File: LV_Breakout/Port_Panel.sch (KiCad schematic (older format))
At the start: 24 parts, among them J1 DB9_Male_MountingHoles, J10 TE 776228-1, J2 B3B-PH-K-S(LF)(SN), J3 Conn_02x03_Odd_Even, J4 LD09S13A4GX00LF, J5 USB_B, J6 RJ45, J7 B6B-XH-A(LF)(SN), J8 B10B-PHDSS(LF)(SN), J9 RJ45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

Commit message: change port panel
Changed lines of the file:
@@
 	9425 2775 8750 2775
 Wire Wire Line
+	10050 2125 10625 2125
+Wire Wire Line
+	10050 2925 10625 2925
+Wire Wire Line
 	10050 1325 10625 1325
 Wire Wire Line
-	10050 1225 10625 1225
-Wire Wire Line
-	10050 1125 10625 1125
-Wire Wire Line
-	10050 1025 10625 1025
-Wire Wire Line
-	10625 925  10050 925
-Wire Wire Line
-	10625 825  10050 825
-Text Label 10050 825  0    50   ~ 0
+	10050 2025 10625 2025
+Wire Wire Line
+	10625 2825 10050 2825
+Wire Wire Line
+	10625 2725 10050 2725
+Text Label 10050 2725 0    50   ~ 0
 Sensor_1
-Text Label 10050 925  0    50   ~ 0
+Text Label 10050 2825 0    50   ~ 0
 Sensor_2
-Text Label 10050 1025 0    50   ~ 0
+Text Label 10050 2025 0    50   ~ 0
 Sensor_3
-Text Label 10050 1125 0    50   ~ 0
+Text Label 10050 1325 0    50   ~ 0
 Sensor_4
-Text Label 10050 1225 0    50   ~ 0
+Text Label 10050 2925 0    50   ~ 0
 Sensor_5
-Text Label 10050 1325 0    50   ~ 0
+Text Label 10050 2125 0    50   ~ 0
 Sensor_6
 Text Label 3000 2675 2    50   ~ 0
@@
 Sensor_7
 Wire Wire Line
-	10625 1625 10050 1625
-Text Label 10050 1825 0    50   ~ 0
+	10625 2225 10050 2225
+Text Label 10050 2625 0    50   ~ 0
 CAN+
 Wire Wire Line
@@
 	10050 1525 10625 1525
 Wire Wire Line
-	10050 1725 10625 1725
-Text Label 10050 1725 0    50   ~ 0
+	10050 3025 10625 3025
+Text Label 10050 3025 0    50   ~ 0
 Sensor_10
-Text Label 10050 1625 0    50   ~ 0
+Text Label 10050 2225 0    50   ~ 0
 Sensor_9
 Text Label 10050 1525 0    50   ~ 0
@@
 Sensor_7
 Wire Wire Line
-	10050 1825 10625 1825
-Text Label 10050 2025 0    50   ~ 0
+	10050 2625 10625 2625
+Text Label 10050 2525 0    50   ~ 0
 CAN-
 Wire Wire Line
@@
 L power:GND #PWR026
 U 1 1 5E62FDAB
-P 10275 3025
-F 0 "#PWR026" H 10275 2775 50  0001 C CNN
-F 1 "GND" H 10280 2852 50  0000 C CNN
-F 2 "" H 10275 3025 50  0001 C CNN
-F 3 "" H 10275 3025 50  0001 C CNN
-	1    10275 3025
-	1    0    0    -1
-$EndComp
-Wire Wire Line
-	10275 3025 10625 3025
-Wire Wire Line
-	10625 2925 10275 2925
-Wire Wire Line
-	10275 2925 10275 3025
-Connection ~ 10275 3025
-Wire Wire Line
-	10625 2825 10275 2825
-Wire Wire Line
-	10275 2825 10275 2925
-Connection ~ 10275 2925
-Wire Wire Line
-	10625 2725 10275 2725
-Wire Wire Line
-	10275 2725 10275 2825
-Connection ~ 10275 2825
+P 9875 1225
+F 0 "#PWR026" H 9875 975 50  0001 C CNN
+F 1 "GND" H 9880 1052 50  0000 C CNN
+F 2 "" H 9875 1225 50  0001 C CNN
+F 3 "" H 9875 1225 50  0001 C CNN
+	1    9875 1225
+	1    0    0    -1
+$EndComp
+Wire Wire Line
+	9875 1225 10625 1225
+Wire Wire Line
+	10625 1125 9875 1125
+Wire Wire Line
+	9875 1125 9875 1225
+Connection ~ 9875 1225
+Wire Wire Line
+	10625 1025 9875 1025
+Wire Wire Line
+	9875 1025 9875 1125
+Connection ~ 9875 1125
+Wire Wire Line
+	10625 925  9875 925
+Wire Wire Line
+	9875 925  9875 1025
+Connection ~ 9875 1025
+Text Label 10050 2425 0    50   ~ 0
+RINEHART_RX
+Wire Wire Line
+	10050 2425 10625 2425
 Text Label 10050 2325 0    50   ~ 0
-RINEHART_RX
+RINEHART_TX
 Wire Wire Line
 	10050 2325 10625 2325
-Text Label 10050 2225 0    50   ~ 0
-RINEHART_TX
-Wire Wire Line
-	10050 2225 10625 2225
-Text Label 10050 2425 0    50   ~ 0
+Text Label 10050 1725 0    50   ~ 0
 BMS_FAULT
 Wire Wire Line
-	10050 2425 10625 2425
+	10050 1725 10625 1725
 Text Label 10050 1925 0    50   ~ 0
 CAN+
 Wire Wire Line
-	10050 2025 10625 2025
-Text Label 10050 2125 0    50   ~ 0
+	10050 2525 10625 2525
+Text Label 10050 1825 0    50   ~ 0
 CAN-
 Wire Wire Line
-	10050 2125 10625 2125
+	10050 1825 10625 1825
 $Comp
 L Connector_Generic:Conn_01x06 J7
@@
 Text Notes 5975 750  0    50   ~ 0
 Serial Port\nfor RineHart
-Text Notes 10325 725  0    50   ~ 0
+Text Notes 11625 675  0    50   ~ 0
 Main Ampseal
-Text Label 10050 2525 0    50   ~ 0
+Text Label 10050 1625 0    50   ~ 0
 EMUS_TX+
-Text Label 10050 2625 0    50   ~ 0
+Text Label 10050 825  0    50   ~ 0
 EMUS_TX-
-Text Notes 11075 2625 0    50   ~ 0
+Text Notes 10825 3550 0    50   ~ 0
 EMUS TX- is for \nEMUS Current Monitor RX
 Wire Wire Line
-	10625 2525 10050 2525
-Wire Wire Line
-	10625 2625 10050 2625
+	10625 1625 10050 1625
+Wire Wire Line
+	10625 825  10050 825
 $Comp
 L Device:R R1

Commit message: Updated PCB Layout
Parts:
- added Q1: PSMN5R2-60YL, Package_TO_SOT_SMD:LFPAK56, symbol Transistor_FET:PSMN5R2-60YL
- added R5: 100, Resistor_SMD:R_0603_1608Metric_Pad1.05x0.95mm_HandSolder, symbol Device:R
- J8: value B10B-PHDSS(LF)(SN) -> B12B-PUDSS-1(LF)(SN); footprint Connector_JST:JST_PHD_B10B-PHDSS_2x05_P2.00mm_Vertical -> Connector_JST:JST_PHD_B12B-PHDSS_2x06_P2.00mm_Vertical; symbol Connector_Generic:Conn_02x05_Counter_Clockwise -> Connector_Generic:Conn_02x06_Counter_Clockwise
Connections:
- net labels added: EMUS_Curr1, EMUS_Curr2, EMUS_Curr3, FAN_OUT, FAN_SIG
- net labels removed: BMS_USB_GND, EMUS_TX+, EMUS_TX-, Sensor_10, Sensor_9
- wire segments 137 -> 146
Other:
- note added: "fan control\n"
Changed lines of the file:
@@
 	3000 2475 2600 2475
-Wire Wire Line
-	3000 2575 2600 2575
 Wire Wire Line
 	3000 2675 2600 2675
@@
 $EndComp
 $Comp
-L Connector_Generic:Conn_02x05_Counter_Clockwise J8
+L Connector_Generic:Conn_02x06_Counter_Clockwise J8
 U 1 1 5E5B056E
 P 8450 2775
 F 0 "J8" H 8500 3192 50  0000 C CNN
-F 1 "B10B-PHDSS(LF)(SN)" H 8500 3101 50  0000 C CNN
-F 2 "Connector_JST:JST_PHD_B10B-PHDSS_2x05_P2.00mm_Vertical" H 8450 2775 50  0001 C CNN
+F 1 "B12B-PUDSS-1(LF)(SN)" H 8500 3101 50  0000 C CNN
+F 2 "Connector_JST:JST_PHD_B12B-PHDSS_2x06_P2.00mm_Vertical" H 8450 2775 50  0001 C CNN
 F 3 "~" H 8450 2775 50  0001 C CNN
 	1    8450 2775
 	1    0    0    -1
 $EndComp
+Wire Wire Line
+	7650 2575 8250 2575
 Text Label 7650 2575 0    50   ~ 0
-BMS_USB_GND
-Wire Wire Line
-	7650 2575 8250 2575
+BMS_USB+
+Wire Wire Line
+	7650 2675 8250 2675
 Text Label 7650 2675 0    50   ~ 0
-BMS_USB+
-Wire Wire Line
-	7650 2675 8250 2675
-Text Label 7650 2775 0    50   ~ 0
 BMS_USB-
 Wire Wire Line
 	7650 2775 8250 2775
-Text Label 7650 2875 0    50   ~ 0
+Text Label 9275 3075 2    50   ~ 0
 BMS_FAULT
-Wire Wire Line
-	7650 2875 8250 2875
 Text Label 7650 2975 0    50   ~ 0
 CAN+
@@
 L power:GND #PWR025
 U 1 1 5E5C1626
-P 9425 2775
-F 0 "#PWR025" H 9425 2525 50  0001 C CNN
-F 1 "GND" H 9430 2602 50  0000 C CNN
-F 2 "" H 9425 2775 50  0001 C CNN
-F 3 "" H 9425 2775 50  0001 C CNN
-	1    9425 2775
-	1    0    0    -1
-$EndComp
-Text Label 9275 2875 2    50   ~ 0
+P 7550 3075
+F 0 "#PWR025" H 7550 2825 50  0001 C CNN
+F 1 "GND" H 7555 2902 50  0000 C CNN
+F 2 "" H 7550 3075 50  0001 C CNN
+F 3 "" H 7550 3075 50  0001 C CNN
+	1    7550 3075
+	1    0    0    -1
+$EndComp
+Text Label 7650 2775 0    50   ~ 0
 CAN-
 Wire Wire Line
@@
 Wire Wire Line
 	10625 2725 10050 2725
-Text Label 10050 2725 0    50   ~ 0
+Text Label 10050 2825 0    50   ~ 0
 Sensor_1
-Text Label 10050 2825 0    50   ~ 0
+Text Label 10050 2225 0    50   ~ 0
 Sensor_2
 Text Label 10050 2025 0    50   ~ 0
@@
 Text Label 10050 2125 0    50   ~ 0
 Sensor_6
-Text Label 3000 2675 2    50   ~ 0
-Sensor_10
-Text Label 3000 2575 2    50   ~ 0
-Sensor_9
 Text Label 3000 2475 2    50   ~ 0
 Sensor_8
@@
 Wire Wire Line
 	10050 3025 10625 3025
-Text Label 10050 3025 0    50   ~ 0
-Sensor_10
-Text Label 10050 2225 0    50   ~ 0
-Sensor_9
 Text Label 10050 1525 0    50   ~ 0
 Sensor_8
-Text Label 10050 1425 0    50   ~ 0
-Sensor_7
 Wire Wire Line
 	10050 2625 10625 2625
-Text Label 10050 2525 0    50   ~ 0
+Text Label 10050 2725 0    50   ~ 0
 CAN-
 Wire Wire Line
@@
 	9875 925  9875 1025
 Connection ~ 9875 1025
-Text Label 10050 2425 0    50   ~ 0
+Text Label 10050 1625 0    50   ~ 0
 RINEHART_RX
 Wire Wire Line
 	10050 2425 10625 2425
-Text Label 10050 2325 0    50   ~ 0
+Text Label 10050 825  0    50   ~ 0
 RINEHART_TX
 Wire Wire Line
 	10050 2325 10625 2325
-Text Label 10050 1725 0    50   ~ 0
+Text Label 10050 2525 0    50   ~ 0
 BMS_FAULT
 Wire Wire Line
 	10050 1725 10625 1725
+Text Label 10050 1825 0    50   ~ 0
+CAN+
+Wire Wire Line
+	10050 2525 10625 2525
 Text Label 10050 1925 0    50   ~ 0
-CAN+
-Wire Wire Line
-	10050 2525 10625 2525
-Text Label 10050 1825 0    50   ~ 0
 CAN-
 Wire Wire Line
@@
 L power:+12V #PWR024
 U 1 1 5E6CC3D5
-P 9425 2675
-F 0 "#PWR024" H 9425 2525 50  0001 C CNN
-F 1 "+12V" H 9440 2848 50  0000 C CNN
-F 2 "" H 9425 2675 50  0001 C CNN
-F 3 "" H 9425 2675 50  0001 C CNN
-	1    9425 2675
-	1    0    0    -1
-$EndComp
-Wire Wire Line
-	8750 2675 9425 2675
+P 9425 2775
+F 0 "#PWR024" H 9425 2625 50  0001 C CNN
+F 1 "+12V" H 9440 2948 50  0000 C CNN
+F 2 "" H 9425 2775 50  0001 C CNN
+F 3 "" H 9425 2775 50  0001 C CNN
+	1    9425 2775
+	1    0    0    -1
+$EndComp
 Text Label 7950 1275 0    50   ~ 0
 SDA
@@
 Text Notes 5975 750  0    50   ~ 0
 Serial Port\nfor RineHart
-Text Notes 11625 675  0    50   ~ 0
+Text Notes 10100 625  0    50   ~ 0
 Main Ampseal
-Text Label 10050 1625 0    50   ~ 0
-EMUS_TX+
-Text Label 10050 825  0    50   ~ 0
-EMUS_TX-
-Text Notes 10825 3550 0    50   ~ 0
+Text Label 9250 2675 2    50   ~ 0
+EMUS_Curr2
+Text Label 10050 2325 0    50   ~ 0
+EMUS_Curr1
+Text Notes 10100 3375 0    50   ~ 0
 EMUS TX- is for \nEMUS Current Monitor RX
 Wire Wire Line
@@
 Wire Wire Line
 	2975 2175 2600 2175
+Text Notes 8200 5475 0    50   ~ 0
+fan control\n
+Text Label 3000 2675 2    50   ~ 0
+FAN_SIG
+Text Label 8025 5675 0    50   ~ 0
+FAN_SIG
+Wire Wire Line
+	8025 5675 8475 5675
+$Comp
+L Device:R R5
+U 1 1 5E5C2565
+P 8475 5825
+F 0 "R5" H 8545 5871 50  0000 L CNN
+F 1 "100" H 8545 5780 50  0000 L CNN
+F 2 "Resistor_SMD:R_0603_1608Metric_Pad1.05x0.95mm_HandSolder" V 8405 5825 50  0001 C CNN
+F 3 "~" H 8475 5825 50  0001 C CNN
+	1    8475 5825
+	1    0    0    -1
+$EndComp
+Connection ~ 8475 5675
+Wire Wire Line
+	8475 5675 8625 5675
+$Comp
+L power:GND #PWR0101
+U 1 1 5E5C32FB
+P 8925 6100
+F 0 "#PWR0101" H 8925 5850 50  0001 C CNN
+F 1 "GND" H 8930 5927 50  0000 C CNN
+F 2 "" H 8925 6100 50  0001 C CNN
+F 3 "" H 8925 6100 50  0001 C CNN
+	1    8925 6100
+	1    0    0    -1
+$EndComp
+Wire Wire Line
+	8475 5975 8475 6100
+Wire Wire Line
+	8475 6100 8925 6100
+Wire Wire Line
+	8925 6100 8925 5875
+Connection ~ 8925 6100
+Text Label 8925 5250 0    50   ~ 0
+FAN_OUT
+Wire Wire Line
+	8925 5250 8925 5475
+Text Label 10050 3025 0    50   ~ 0
+FAN_OUT
+$Comp
+L Transistor_FET:PSMN5R2-60YL Q1
+U 1 1 5E5DFCCF
+P 8825 5675
+F 0 "Q1" H 9030 5721 50  0000 L CNN
+F 1 "PSMN5R2-60YL" H 9030 5630 50  0000 L CNN
+F 2 "Package_TO_SOT_SMD:LFPAK56" H 8975 5675 50  0001 C CNN
+F 3 "https://assets.nexperia.com/documents/data-sheet/PSMN5R2-60YL.pdf" H 8825 5675 50  0001 C CNN
+	1    8825 5675
+	1    0    0    -1
+$EndComp
+Text Label 10050 1425 0    50   ~ 0
+Sensor_7
+Text Label 10050 2425 0    50   ~ 0
+EMUS_Curr2
+Text Label 9250 2575 2    50   ~ 0
+EMUS_Curr1
+Text Label 10050 1725 0    50   ~ 0
+EMUS_Curr3
+Text Label 9275 2875 2    50   ~ 0
+EMUS_Curr3
+Wire Wire Line
+	9275 3075 8750 3075
+Wire Wire Line
+	9250 2575 8750 2575
+Wire Wire Line
+	9250 2675 8750 2675
+Wire Wire Line
+	7550 3075 8250 3075
+Wire Wire Line
+	7550 2875 7550 3075
+Wire Wire Line
+	7550 2875 8250 2875
+Connection ~ 7550 3075
 $EndSCHEMATC

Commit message: Minor Layout Changes
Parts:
- added C10, C6, C7, C8, C9: 1u, Capacitor_SMD:C_0603_1608Metric_Pad1.05x0.95mm_HandSolder, symbol Device:C
- added J11: 2.54mmPins, Connector_PinHeader_2.54mm:PinHeader_1x03_P2.54mm_Vertical, symbol Connector_Generic:Conn_01x03
- added U4: MAX232, Package_SO:SOIC-16_3.9x9.9mm_P1.27mm, symbol Interface_UART:MAX232
- J1: value DB9_Male_MountingHoles -> 171-009-113R001
- J4: value LD09S13A4GX00LF -> 171-009-213R001
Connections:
- net +12V: now also J1.9
- net +5V: now also C10.1, U4.16 (VCC)
- net BMS_USB+: now also J8.8 (Pin_8); no longer J8.1 (Pin_1)
- net BMS_USB-: now also J8.6 (Pin_6); no longer J8.2 (Pin_2)
- net BMS_USB_5V: now also J8.4 (Pin_4); no longer J8.8 (Pin_8)
- net GND: now also J1.0 (PAD), J1.5, J8.1 (Pin_1), J8.2 (Pin_2), C10.2, C6.2, C7.2, J11.3 (Pin_3), U4.10 (T2IN), U4.15 (GND), U4.8 (R2IN); no longer J8.4 (Pin_4), J8.6 (Pin_6)
- net RXD: now reaches U1.30 (PD0)
- net RXD: now also J11.1 (Pin_1)
- net TXD: now reaches U1.31 (PD1)
- net TXD: now also J11.2 (Pin_2)
- net IMU_RX: now reaches J1.2
- net IMU_RX: now also U4.13 (R1IN)
- net IMU_TX: now reaches J1.3
- net IMU_TX: now also U4.14 (T1OUT)
- net E1_P: now reaches J9.1
- net E1_P: now also J6.1; no longer J6.8
- net E1_N: now reaches J9.2
- net E1_N: now also J6.2; no longer J6.7
- net E3_N: now reaches J6.6
- net E3_N: now also J9.6; no longer J9.3
- net E2_N: now reaches J6.5
- net E2_N: now also J9.5; no longer J9.4
- net E2_P: now reaches J6.4
- net E2_P: now also J9.4; no longer J9.5
- net E3_P: now reaches J6.3
- net E3_P: now also J9.3; no longer J9.6
- net E4_P: now reaches J9.7
- net E4_P: now also J6.7; no longer J6.2
- net E4_N: now reaches J9.8
- net E4_N: now also J6.8; no longer J6.1
- net IMU_TX+ renamed IMU_TX_U
- net IMU_TX_U: now also U4.11 (T1IN)
- net IMU_TX- renamed IMU_RX_U
- net IMU_RX_U: now also U4.12 (R1OUT)
- new net: C8.1, U4.1 (C1+)
- new net: C7.1, U4.2 (VS+)
- new net: C8.2, U4.3 (C1-)
- new net: C9.1, U4.4 (C2+)
- new net: C9.2, U4.5 (C2-)
- new net: C6.1, U4.6 (VS-)
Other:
- note added: "UART for ATMEGA\n"
- moved on the sheet: D1, J1, J2, J4, J5, J6, J7, J9, Q1, R5

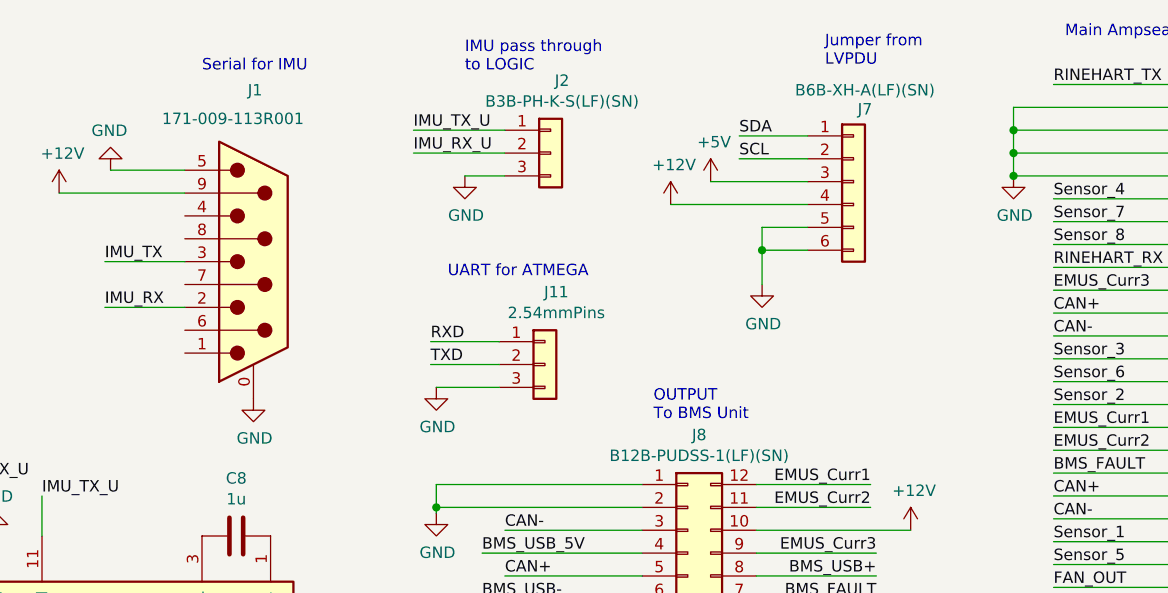
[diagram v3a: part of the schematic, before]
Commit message: Change trace and create Gerber
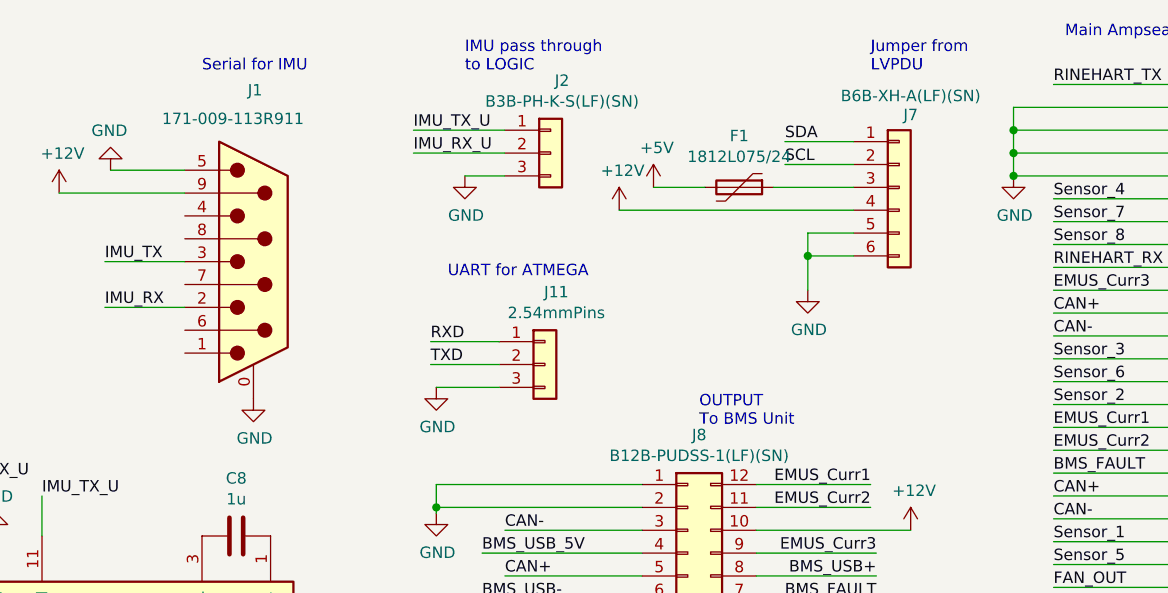
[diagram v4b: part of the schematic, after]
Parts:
- added F1: 1812L075/24, Fuse:Fuse_1812_4532Metric_Pad1.30x3.40mm_HandSolder, symbol Device:Polyfuse
- J1: value 171-009-113R001 -> 171-009-113R911
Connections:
- net +5V: now also F1.2; no longer J7.3 (Pin_3)
- new net: F1.1, J7.3 (Pin_3)
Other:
- moved on the sheet: J7
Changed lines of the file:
@@
 L Connector_Generic:Conn_01x06 J7
 U 1 1 5E685331
-P 9175 1250
-F 0 "J7" H 9225 1567 50  0000 C CNN
-F 1 "B6B-XH-A(LF)(SN)" H 9225 1650 50  0000 C CNN
-F 2 "Connector_JST:JST_PH_B6B-PH-K_1x06_P2.00mm_Vertical" H 9175 1250 50  0001 C CNN
-F 3 "~" H 9175 1250 50  0001 C CNN
-	1    9175 1250
+P 9375 1275
+F 0 "J7" H 9425 1592 50  0000 C CNN
+F 1 "B6B-XH-A(LF)(SN)" H 9425 1675 50  0000 C CNN
+F 2 "Connector_JST:JST_PH_B6B-PH-K_1x06_P2.00mm_Vertical" H 9375 1275 50  0001 C CNN
+F 3 "~" H 9375 1275 50  0001 C CNN
+	1    9375 1275
 	1    0    0    -1
 $EndComp
@@
 L power:+5V #PWR022
 U 1 1 5E68B39B
-P 8550 1250
-F 0 "#PWR022" H 8550 1100 50  0001 C CNN
-F 1 "+5V" H 8565 1423 50  0000 C CNN
-F 2 "" H 8550 1250 50  0001 C CNN
-F 3 "" H 8550 1250 50  0001 C CNN
-	1    8550 1250
+P 8300 1275
+F 0 "#PWR022" H 8300 1125 50  0001 C CNN
+F 1 "+5V" H 8315 1448 50  0000 C CNN
+F 2 "" H 8300 1275 50  0001 C CNN
+F 3 "" H 8300 1275 50  0001 C CNN
+	1    8300 1275
 	1    0    0    -1
 $EndComp
@@
 L power:+12V #PWR021
 U 1 1 5E694921
-P 8375 1350
-F 0 "#PWR021" H 8375 1200 50  0001 C CNN
-F 1 "+12V" H 8390 1523 50  0000 C CNN
-F 2 "" H 8375 1350 50  0001 C CNN
-F 3 "" H 8375 1350 50  0001 C CNN
-	1    8375 1350
+P 8150 1375
+F 0 "#PWR021" H 8150 1225 50  0001 C CNN
+F 1 "+12V" H 8165 1548 50  0000 C CNN
+F 2 "" H 8150 1375 50  0001 C CNN
+F 3 "" H 8150 1375 50  0001 C CNN
+	1    8150 1375
 	1    0    0    -1
 $EndComp
@@
 	1    0    0    -1
 $EndComp
-Text Label 8675 1050 0    50   ~ 0
+Text Label 8875 1075 0    50   ~ 0
 SDA
 Wire Wire Line
-	8675 1050 8975 1050
-Text Label 8675 1150 0    50   ~ 0
+	8875 1075 9175 1075
+Text Label 8875 1175 0    50   ~ 0
 SCL
 Wire Wire Line
-	8675 1150 8975 1150
+	8875 1175 9175 1175
 Text Label 3000 2975 2    50   ~ 0
 SCL
@@
 L power:GND #PWR023
 U 1 1 5E734B03
-P 8775 1700
-F 0 "#PWR023" H 8775 1450 50  0001 C CNN
-F 1 "GND" H 8780 1527 50  0000 C CNN
-F 2 "" H 8775 1700 50  0001 C CNN
-F 3 "" H 8775 1700 50  0001 C CNN
-	1    8775 1700
-	1    0    0    -1
-$EndComp
-Wire Wire Line
-	8775 1550 8775 1700
+P 8975 1725
+F 0 "#PWR023" H 8975 1475 50  0001 C CNN
+F 1 "GND" H 8980 1552 50  0000 C CNN
+F 2 "" H 8975 1725 50  0001 C CNN
+F 3 "" H 8975 1725 50  0001 C CNN
+	1    8975 1725
+	1    0    0    -1
+$EndComp
+Wire Wire Line
+	8975 1575 8975 1725
 Text Notes 9800 3875 0    50   ~ 0
 Pass Through for\nLOGIC Ethernet\n
-Text Notes 9050 750  0    50   ~ 0
+Text Notes 9250 775  0    50   ~ 0
 Jumper from\nLVPDU
-Text Notes 8300 2300 0    50   ~ 0
+Text Notes 8500 2325 0    50   ~ 0
 OUTPUT\nTo BMS Unit
 Text Notes 8375 5150 0    50   ~ 0
@@
 P 6550 1600
 F 0 "J1" H 6525 2350 50  0000 L CNN
-F 1 "171-009-113R001" H 6150 2225 50  0000 L CNN
+F 1 "171-009-113R911" H 6150 2225 50  0000 L CNN
 F 2 "Connector_Dsub:DSUB-9_Male_Vertical_P2.77x2.84mm_MountingHoles" H 6550 1600 50  0001 C CNN
 F 3 " ~" H 6550 1600 50  0001 C CNN
@@
 $EndComp
 Wire Wire Line
-	8775 1550 8975 1550
-Wire Wire Line
-	8775 1550 8775 1450
-Wire Wire Line
-	8775 1450 8975 1450
-Connection ~ 8775 1550
-Wire Wire Line
-	8375 1350 8975 1350
-Wire Wire Line
-	8550 1250 8975 1250
+	8975 1575 9175 1575
+Wire Wire Line
+	8975 1575 8975 1475
+Wire Wire Line
+	8975 1475 9175 1475
+Connection ~ 8975 1575
 $Comp
 L power:GND #PWR012
@@
 Text Notes 7400 1675 0    50   ~ 0
 UART for ATMEGA\n
+$Comp
+L Device:Polyfuse F1
+U 1 1 5E611575
+P 8675 1275
+F 0 "F1" V 8450 1275 50  0000 C CNN
+F 1 "1812L075/24" V 8541 1275 50  0000 C CNN
+F 2 "Fuse:Fuse_1812_4532Metric_Pad1.30x3.40mm_HandSolder" H 8725 1075 50  0001 L CNN
+F 3 "~" H 8675 1275 50  0001 C CNN
+	1    8675 1275
+	0    1    1    0
+$EndComp
+Wire Wire Line
+	8825 1275 9175 1275
+Wire Wire Line
+	8300 1275 8525 1275
+Wire Wire Line
+	8150 1375 9175 1375
 $EndSCHEMATC
